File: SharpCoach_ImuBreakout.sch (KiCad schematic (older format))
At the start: 10 parts, among them J1 INTERFACE, U1 LIS3DH, U2 BMG250

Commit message: Finished PCB trace routing.
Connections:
- wire segments 55 -> 57
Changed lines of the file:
@@
 Text Label 6250 2600 0    50   ~ 0
 CS_ACCEL
-NoConn ~ 8350 2050
-NoConn ~ 8350 2150
-NoConn ~ 8350 2250
-Wire Wire Line
-	8350 2350 9100 2350
-Text Label 9100 2350 2    50   ~ 0
+NoConn ~ 8350 2000
+NoConn ~ 8350 2100
+NoConn ~ 8350 2200
+Wire Wire Line
+	8350 2400 9100 2400
+Text Label 9100 2400 2    50   ~ 0
 INT1_ACCEL
 Wire Wire Line
-	8350 2450 9300 2450
-Wire Wire Line
-	8350 2550 9100 2550
-Text Label 9100 2550 2    50   ~ 0
+	8350 2500 9300 2500
+Wire Wire Line
+	8350 2600 9100 2600
+Text Label 9100 2600 2    50   ~ 0
 INT2_ACCEL
 $Comp
 L power:GND #PWR07
 U 1 1 5B61ABBB
-P 9300 2500
-F 0 "#PWR07" H 9300 2250 50  0001 C CNN
-F 1 "GND" H 9305 2327 50  0000 C CNN
-F 2 "" H 9300 2500 50  0001 C CNN
-F 3 "" H 9300 2500 50  0001 C CNN
-	1    9300 2500
+P 9300 2550
+F 0 "#PWR07" H 9300 2300 50  0001 C CNN
+F 1 "GND" H 9305 2377 50  0000 C CNN
+F 2 "" H 9300 2550 50  0001 C CNN
+F 3 "" H 9300 2550 50  0001 C CNN
+	1    9300 2550
 	1    0    0    -1
 $EndComp
@@
 VIN
 Wire Wire Line
-	9300 2500 9300 2450
+	9300 2550 9300 2500
 Wire Wire Line
 	1850 2000 1850 1900
@@
 $EndComp
 Connection ~ 5300 2300
+Wire Wire Line
+	8350 2300 9300 2300
+Wire Wire Line
+	9300 2300 9300 2500
+Connection ~ 9300 2500
 $EndSCHEMATC

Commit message: Updated library paths to use submodules.
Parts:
- removed C4: 10u, Capacitor_SMD:C_0805_2012Metric_Pad1.15x1.40mm_HandSolder, symbol Device:C
- removed J1: INTERFACE, Connector_PinHeader_2.54mm:PinHeader_2x07_P2.54mm_Vertical, symbol Connector_Generic:Conn_02x07_Odd_Even
- removed JP1: Jumper SPI MOSI, Connector_PinHeader_2.54mm:PinHeader_1x02_P2.54mm_Vertical, symbol Jumper:Jumper_2_Open
- removed JP2: Jumper SPI MISO, Connector_PinHeader_2.54mm:PinHeader_1x02_P2.54mm_Vertical, symbol Jumper:Jumper_2_Open
- removed JP3: Jumper SPI CLK, Connector_PinHeader_2.54mm:PinHeader_1x02_P2.54mm_Vertical, symbol Jumper:Jumper_2_Open
- removed U1: LIS3DH, LIS3DH:LIS3DH, symbol LIS3DH:LIS3DH
- removed U2: BMG250, BMG250:BMG250, symbol BMG250:BMG250
- added J1: PMOD_Type2A_Variant01, PMOD_SpecB:PMOD_SpecB, symbol PMOD_Type2A_Variant01:PMOD_Type2A_Variant01
- added R1, R2: 10k, Resistor_SMD:R_0603_1608Metric_Pad1.05x0.95mm_HandSolder, symbol Device:R
- added U1: LSM6DS33, LSM6DS33:LSM6DS33, symbol LSM6DS33:LSM6DS33
- C1: value 10u -> 100n; footprint Capacitor_SMD:C_0805_2012Metric_Pad1.15x1.40mm_HandSolder -> Capacitor_SMD:C_0603_1608Metric_Pad1.05x0.95mm_HandSolder
- C3: value 100n -> 1u
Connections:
- net labels added: INT1, INT2, MISO, MOSI, SCK, SS, VCC
- net labels removed: CLK_ACCEL, CLK_GYRO, CS_ACCEL, CS_GYRO, INT1_ACCEL, INT1_GYRO, INT2_ACCEL, INT2_GYRO, MISO_ACCEL, MISO_GYRO, MOSI_ACCEL, MOSI_GYRO, VIN
- wire segments 57 -> 62
- no-connect marks 7 -> 1

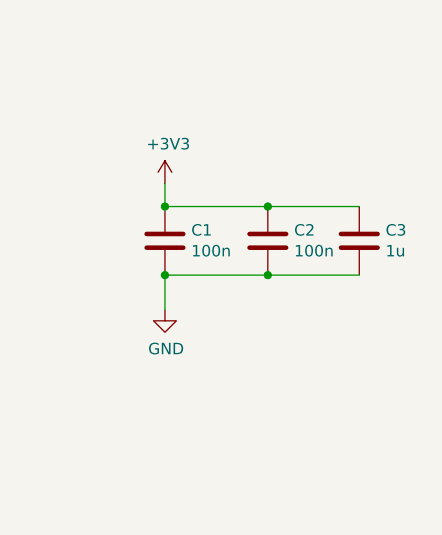
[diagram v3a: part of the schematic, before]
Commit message: Updated symbol and footprint libraries to use submodules
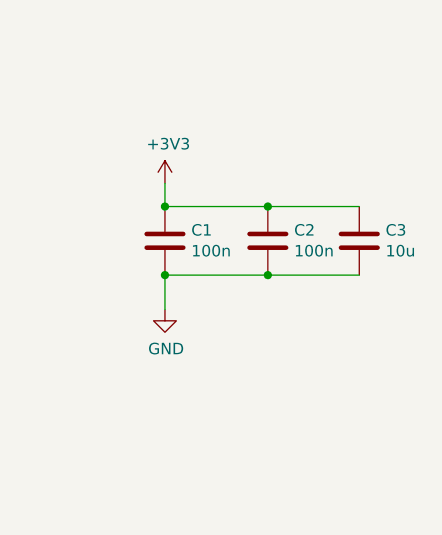
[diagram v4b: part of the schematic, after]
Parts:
- C3: value 1u -> 10u
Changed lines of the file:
@@
 P 9250 3650
 F 0 "C3" H 9365 3696 50  0000 L CNN
-F 1 "1u" H 9365 3605 50  0000 L CNN
+F 1 "10u" H 9365 3605 50  0000 L CNN
 F 2 "Capacitor_SMD:C_0603_1608Metric_Pad1.05x0.95mm_HandSolder" H 9288 3500 50  0001 C CNN
 F 3 "~" H 9250 3650 50  0001 C CNN
